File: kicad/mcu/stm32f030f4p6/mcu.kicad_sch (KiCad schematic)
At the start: 28 parts, among them J1 Conn_01x05, J2 Conn_01x04, Q1 BC817, U1 LM1117-3.3, U2 STM32F030F4P6

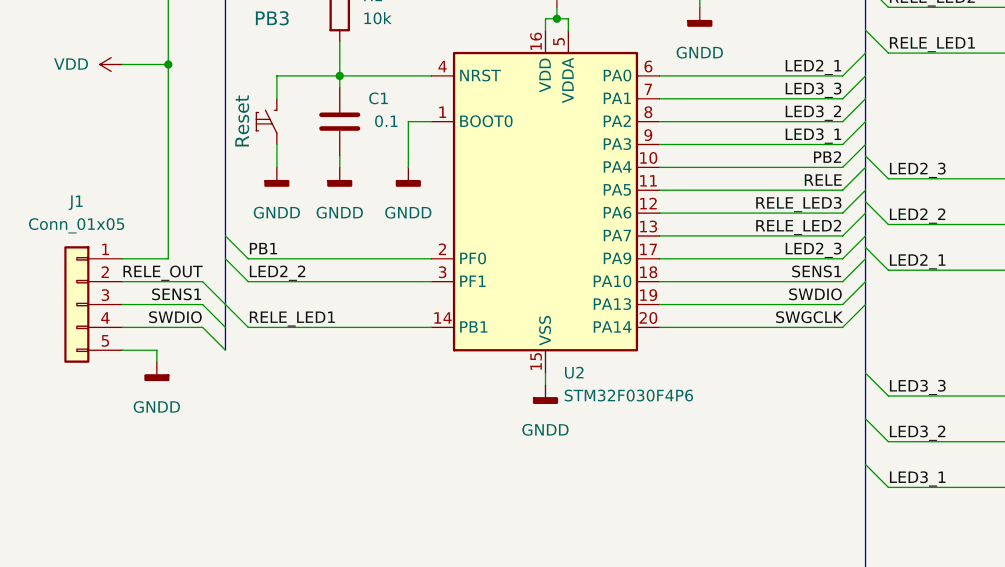
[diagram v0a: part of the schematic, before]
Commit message: Сенсоры перепутал-поправил. Усправил выход у Реле с OD на PP
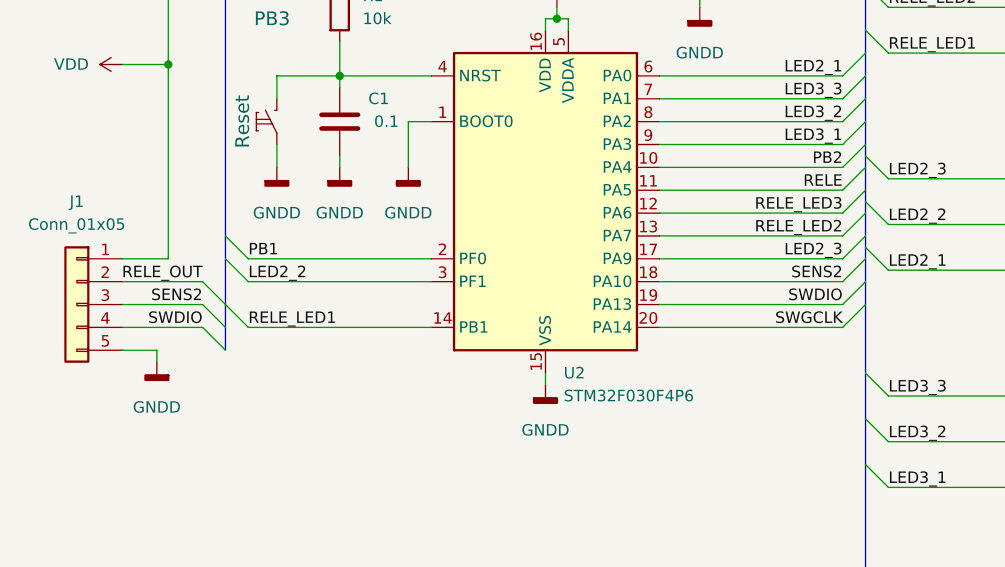
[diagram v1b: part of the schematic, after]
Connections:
- net SENS1 renamed SENS2
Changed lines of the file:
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@@
     (effects (font (size 1.27 1.27)) (justify left bottom))
   )
-  (label "SENS1" (at 107.95 101.6 180)
+  (label "SENS2" (at 107.95 101.6 180)
     (effects (font (size 1.27 1.27)) (justify right bottom))
   )
@@
     (effects (font (size 1.27 1.27)) (justify left bottom))
   )
-  (label "SENS1" (at 179.07 99.06 180)
+  (label "SENS2" (at 179.07 99.06 180)
     (effects (font (size 1.27 1.27)) (justify right bottom))
   )

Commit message: Добавил информаию по корпусу
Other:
- note added: "Корпус D2MG Цена 310р. https://www.chipdip.ru/product/d2mg?from=suggest_product"
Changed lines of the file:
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@@
     (stroke (width 0) (type default) (color 0 0 0 0))
+  )
+  (text "Корпус D2MG\nЦена 310р.\nhttps://www.chipdip.ru/product/d2mg?from=suggest_product\n"
+    (at 26.035 186.055 0)
+    (effects (font (size 1.27 1.27)) (justify left bottom))
   )
   (text "RGB LED 5mA\nR - 1,88V R = 224 Om\nG - 2,48V R = 104 Om\nB - 2,68V R = 64 Om"

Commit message: Косметика
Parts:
- removed J2: Conn_01x04, Connector_JST:JST_EH_B4B-EH-A_1x04_P2.50mm_Vertical, symbol Connector_Generic:Conn_01x04
- added J2: SWD, Connector_JST:JST_EH_B5B-EH-A_1x05_P2.50mm_Vertical, symbol Connector_Generic:Conn_01x05
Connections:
- net GNDD: now also J2.3 (Pin_3)
- net SWDIO: now also J2.2 (Pin_2)
- net SWGCLK: now also J2.4 (Pin_4)
- net VDD: now also J2.5 (Pin_5)
- net at C1.2, PB3.1, R1.2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: now also J2.1 (Pin_1)
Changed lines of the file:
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@@
   (junction (at 212.09 49.53) (diameter 0) (color 0 0 0 0)
   )
+  (junction (at 116.205 76.2) (diameter 0) (color 0 0 0 0)
+  )
   (junction (at 146.685 142.24) (diameter 0) (color 0 0 0 0)
   )
@@
     (stroke (width 0) (type default) (color 0 0 0 0))
   )
+  (wire (pts (xy 99.06 50.8) (xy 106.045 50.8))
+    (stroke (width 0) (type default) (color 0 0 0 0))
+  )
   (bus (pts (xy 181.61 101.6) (xy 181.61 109.22))
     (stroke (width 0) (type default) (color 0 0 0 0))
@@
     (stroke (width 0) (type default) (color 0 0 0 0))
   )
+  (wire (pts (xy 116.205 47.625) (xy 116.205 76.2))
+    (stroke (width 0) (type default) (color 0 0 0 0))
+  )
   (bus (pts (xy 181.61 78.74) (xy 181.61 81.28))
     (stroke (width 0) (type default) (color 0 0 0 0))
@@
     (stroke (width 0) (type default) (color 0 0 0 0))
   )
+  (wire (pts (xy 106.045 50.8) (xy 106.045 47.625))
+    (stroke (width 0) (type default) (color 0 0 0 0))
+  )
   (wire (pts (xy 158.75 91.44) (xy 179.07 91.44))
     (stroke (width 0) (type default) (color 0 0 0 0))
@@
   )
   (wire (pts (xy 140.335 142.24) (xy 144.145 142.24))
+    (stroke (width 0) (type default) (color 0 0 0 0))
+  )
+  (wire (pts (xy 106.045 47.625) (xy 116.205 47.625))
     (stroke (width 0) (type default) (color 0 0 0 0))
   )
@@
     (pin "4")
     (pin "5")
-  )
-  (symbol (lib_id "Connector_Generic:Conn_01x04") (at 93.98 55.88 0) (mirror y) (unit 1)
-    (in_bom yes) (on_board yes) (fields_autoplaced)
-    (property "Reference" "J2" (id 0) (at 93.98 46.99 0))
-    (property "Value" "Conn_01x04" (id 1) (at 93.98 49.53 0))
-    (property "Footprint" "Connector_JST:JST_EH_B4B-EH-A_1x04_P2.50mm_Vertical" (id 2) (at 93.98 55.88 0)
-      (effects (font (size 1.27 1.27)) hide)
-    )
-    (property "Datasheet" "~" (id 3) (at 93.98 55.88 0)
-      (effects (font (size 1.27 1.27)) hide)
-    )
-    (pin "1")
-    (pin "2")
-    (pin "3")
-    (pin "4")
   )
   (symbol (lib_id "Device:LED_RKGB") (at 220.98 116.84 180) (unit 1)
@@
   (symbol (lib_id "кнопки:кнопка") (at 116.205 83.82 90) (unit 1)
     (in_bom yes) (on_board yes)
-    (property "Reference" "PB3" (id 0) (at 113.665 69.85 90)
+    (property "Reference" "PB3" (id 0) (at 116.84 74.295 90)
       (effects (font (size 1.524 1.524)) (justify right))
     )
@@
     (pin "2")
   )
+  (symbol (lib_id "Connector_Generic:Conn_01x05") (at 93.98 55.88 0) (mirror y) (unit 1)
+    (in_bom yes) (on_board yes) (fields_autoplaced)
+    (property "Reference" "J2" (id 0) (at 93.98 44.45 0))
+    (property "Value" "SWD" (id 1) (at 93.98 46.99 0))
+    (property "Footprint" "Connector_JST:JST_EH_B5B-EH-A_1x05_P2.50mm_Vertical" (id 2) (at 93.98 55.88 0)
+      (effects (font (size 1.27 1.27)) hide)
+    )
+    (property "Datasheet" "~" (id 3) (at 93.98 55.88 0)
+      (effects (font (size 1.27 1.27)) hide)
+    )
+    (pin "1")
+    (pin "2")
+    (pin "3")
+    (pin "4")
+    (pin "5")
+  )
   (symbol (lib_id "Device:R") (at 201.93 116.84 90) (unit 1)
     (in_bom yes) (on_board yes)
@@
       (reference "J1") (unit 1) (value "Conn_01x05") (footprint "Connector_JST:JST_EH_B5B-EH-A_1x05_P2.50mm_Vertical")
     )
-    (path "/0acc3c23-b1de-4dfa-8e88-efadfaa43ecd"
-      (reference "J2") (unit 1) (value "Conn_01x04") (footprint "Connector_JST:JST_EH_B4B-EH-A_1x04_P2.50mm_Vertical")
+    (path "/dfd72814-e22f-433b-aa86-d1294424296a"
+      (reference "J2") (unit 1) (value "SWD") (footprint "Connector_JST:JST_EH_B5B-EH-A_1x05_P2.50mm_Vertical")
     )
     (path "/bc159e88-0aca-4651-b852-bd6f007f7779"

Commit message: Детали, стоимость
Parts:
- C1, C2, C4, C5: Aliexpress (none) -> https://www.chipdip.ru/product0/9000649656; ChipDip (none) -> https://www.chipdip.ru/product0/9000649656; Цена (none) -> 6; Цена 2 (none) -> 6
- C3, C6: Aliexpress (none) -> https://www.chipdip.ru/product/tecap-100-mkf-6.3-v-tip-c-10; ChipDip (none) -> https://www.chipdip.ru/product/tecap-100-mkf-6.3-v-tip-c-10; Цена (none) -> 31; Цена 2 (none) -> 31
- D1, D2, D3: Aliexpress (none) -> https://aliexpress.ru/item/1005004567358995.html?sku_id=120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; ChipDip (none) -> https://aliexpress.ru/item/1005004567358995.html?sku_id=120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; Цена (none) -> =140/10; Цена 2 (none) -> =140/10
- J1: Aliexpress (none) -> https://aliexpress.ru/item/1005004837211340.html?sku_id=120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; ChipDip (none) -> https://aliexpress.ru/item/1005004837211340.html?sku_id=120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; Цена (none) -> =160/5; Цена 2 (none) -> =160/5
- J2, PB3: Цена (none) -> 0; Цена 2 (none) -> 0
- PB1, PB2: Aliexpress (none) -> https://www.chipdip.ru/product/kls7-ts6601-11.0-180-it-1102k; ChipDip (none) -> https://www.chipdip.ru/product/kls7-ts6601-11.0-180-it-1102k; Цена (none) -> 9; Цена 2 (none) -> 9
- Q1: Aliexpress (none) -> https://www.chipdip.ru/product/bc817-16-hottech; ChipDip (none) -> https://www.chipdip.ru/product/bc817-16-hottech; Цена 2 (none) -> 4
- R1, R10, R11, R2, R3, R4, R5, R6, R7, R8, R9: Aliexpress (none) -> https://aliexpress.ru/item/1005001794416354.html?sku_id=120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; ChipDip (none) -> https://aliexpress.ru/item/1005001794416354.html?sku_id=120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; Цена (none) -> =47/100; Цена 2 (none) -> =47/100
- U1: Aliexpress (none) -> https://www.chipdip.ru/product/lm1117gs-3.3; ChipDip (none) -> https://www.chipdip.ru/product/lm1117gs-3.3; Цена 2 (none) -> 21
- U2: Aliexpress (none) -> https://aliexpress.ru/item/1005006074715370.html?sku_id=120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; ChipDip (none) -> https://www.chipdip.ru/product/stm32f030f4p6tr-2?from=sugge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; Цена 2 (none) -> =800/10
